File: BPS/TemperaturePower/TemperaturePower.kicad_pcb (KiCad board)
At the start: 2 copper layers, 35 x 44 mm, 7 parts, among them J1 Conn_02x10_Counter_Clockwise, J2 Conn_01x02, J3 Conn_02x10_Counter_Clockwise

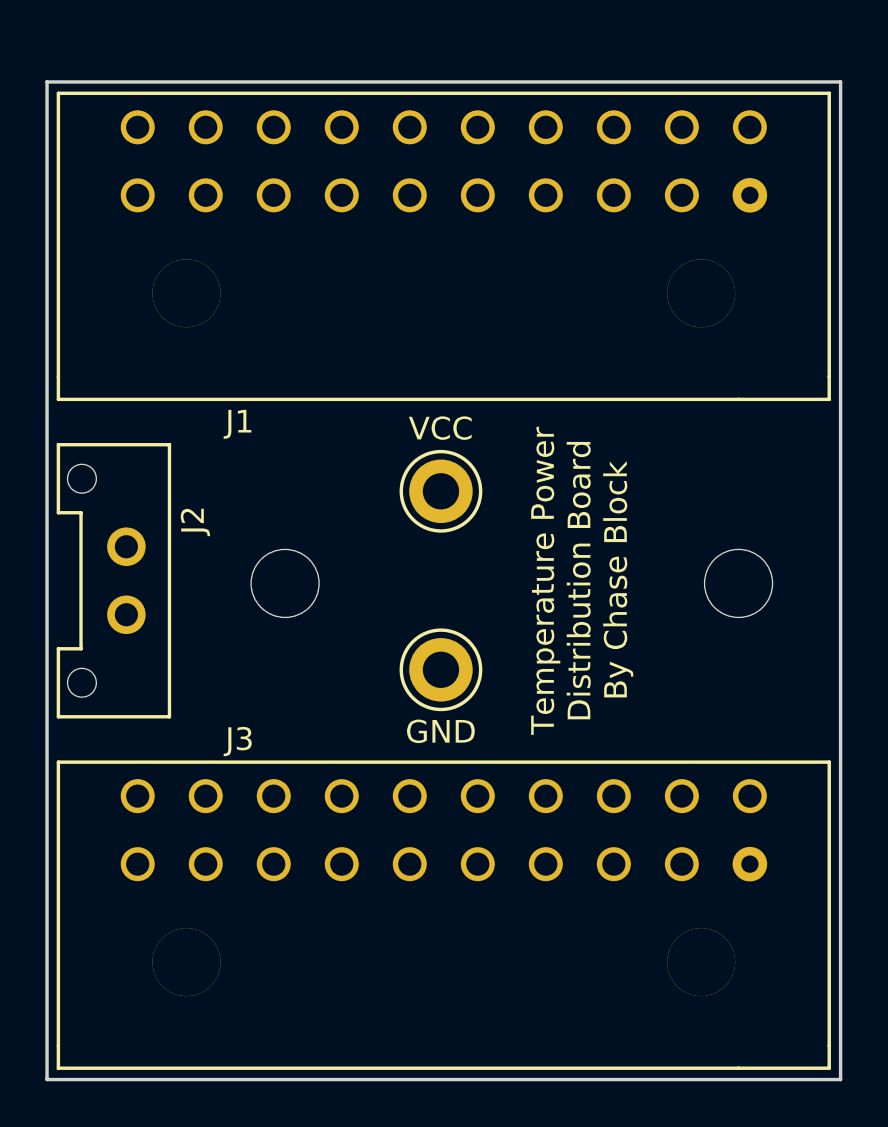
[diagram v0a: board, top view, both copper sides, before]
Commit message: Fix the backwardness to the Temperature power board
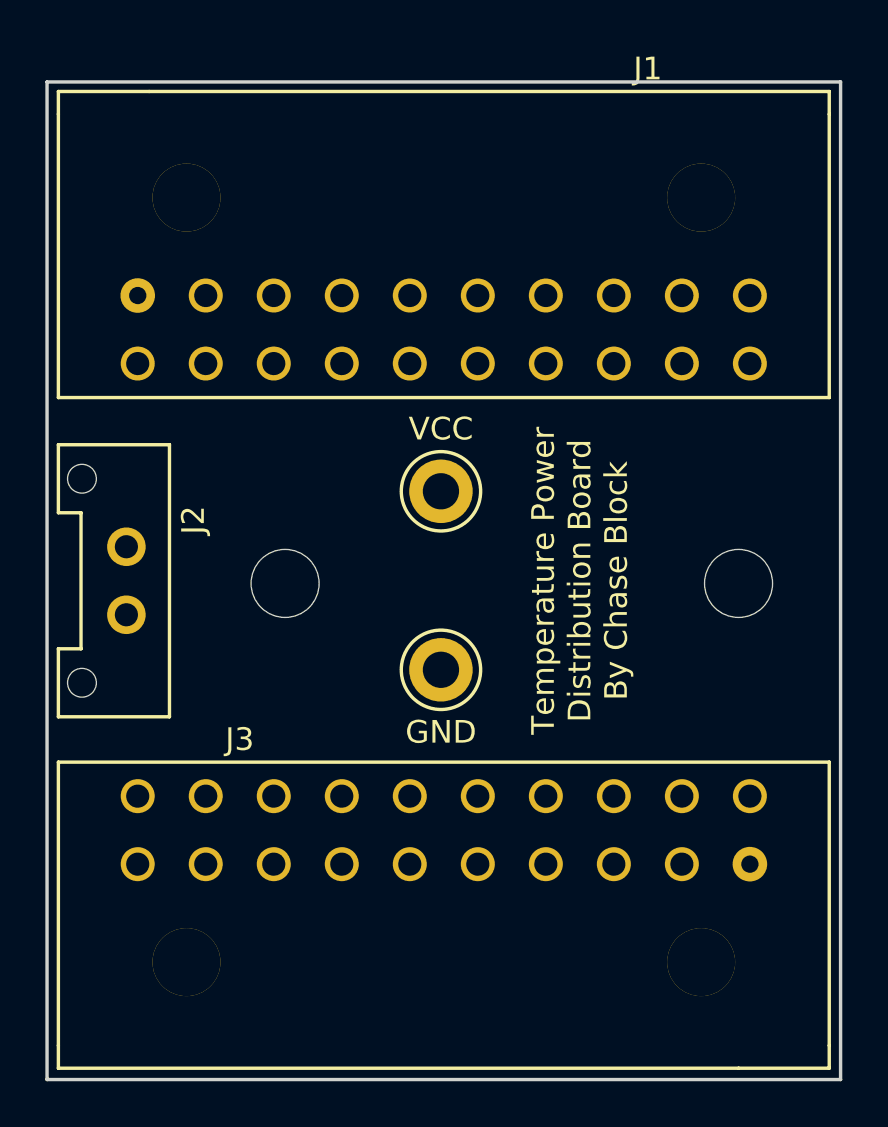
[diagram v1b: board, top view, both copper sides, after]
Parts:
- moved J1 7.42 mm to (135.0, 107.4), turned to 180 degrees
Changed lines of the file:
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@@
-(kicad_pcb (version 20171130) (host pcbnew "(5.1.4)-1")
+(kicad_pcb (version 20171130) (host pcbnew 5.1.4-e60b266~84~ubuntu19.04.1)
   (general
     (thickness 1.6)
@@
   )
   (module UTSVT_Connectors:Molex2x10_horizontal (layer F.Cu)
-    (at 135 100)
+    (at 135 107.42 180)
     (fp_text reference J1 (at -9 11.5) (layer F.SilkS)
       (effects (font (size 1 1) (thickness 0.15)))
@@
     (fp_line (start 13 10.5) (end -17 10.5) (layer F.SilkS) (width 0.15))
     (fp_line (start -17 10.5) (end -17 9.5) (layer F.SilkS) (width 0.15))
-    (pad 1 thru_hole circle (at 13.5 1.5) (size 1.524 1.524) (drill 0.762) (layers *.Cu *.Mask)
+    (pad 1 thru_hole circle (at 13.5 1.5 180) (size 1.524 1.524) (drill 0.762) (layers *.Cu *.Mask)
       (net 1 VCC))
-    (pad 2 thru_hole circle (at 10.5 1.5) (size 1.5 1.5) (drill 1.02) (layers *.Cu *.Mask)
+    (pad 2 thru_hole circle (at 10.5 1.5 180) (size 1.5 1.5) (drill 1.02) (layers *.Cu *.Mask)
       (net 1 VCC))
-    (pad 3 thru_hole circle (at 7.5 1.5) (size 1.5 1.5) (drill 1.02) (layers *.Cu *.Mask)
+    (pad 3 thru_hole circle (at 7.5 1.5 180) (size 1.5 1.5) (drill 1.02) (layers *.Cu *.Mask)
       (net 1 VCC))
-    (pad 4 thru_hole circle (at 4.5 1.5) (size 1.5 1.5) (drill 1.02) (layers *.Cu *.Mask)
+    (pad 4 thru_hole circle (at 4.5 1.5 180) (size 1.5 1.5) (drill 1.02) (layers *.Cu *.Mask)
       (net 1 VCC))
-    (pad 5 thru_hole circle (at 1.5 1.5) (size 1.5 1.5) (drill 1.02) (layers *.Cu *.Mask)
+    (pad 5 thru_hole circle (at 1.5 1.5 180) (size 1.5 1.5) (drill 1.02) (layers *.Cu *.Mask)
       (net 1 VCC))
-    (pad 6 thru_hole circle (at -1.5 1.5) (size 1.5 1.5) (drill 1.02) (layers *.Cu *.Mask)
+    (pad 6 thru_hole circle (at -1.5 1.5 180) (size 1.5 1.5) (drill 1.02) (layers *.Cu *.Mask)
       (net 1 VCC))
-    (pad 7 thru_hole circle (at -4.5 1.5) (size 1.5 1.5) (drill 1.02) (layers *.Cu *.Mask)
+    (pad 7 thru_hole circle (at -4.5 1.5 180) (size 1.5 1.5) (drill 1.02) (layers *.Cu *.Mask)
       (net 1 VCC))
-    (pad 8 thru_hole circle (at -7.5 1.5) (size 1.5 1.5) (drill 1.02) (layers *.Cu *.Mask)
+    (pad 8 thru_hole circle (at -7.5 1.5 180) (size 1.5 1.5) (drill 1.02) (layers *.Cu *.Mask)
       (net 1 VCC))
-    (pad 9 thru_hole circle (at -10.5 1.5) (size 1.5 1.5) (drill 1.02) (layers *.Cu *.Mask)
+    (pad 9 thru_hole circle (at -10.5 1.5 180) (size 1.5 1.5) (drill 1.02) (layers *.Cu *.Mask)
       (net 1 VCC))
-    (pad 10 thru_hole circle (at -13.5 1.5) (size 1.5 1.5) (drill 1.02) (layers *.Cu *.Mask)
+    (pad 10 thru_hole circle (at -13.5 1.5 180) (size 1.5 1.5) (drill 1.02) (layers *.Cu *.Mask)
       (net 1 VCC))
-    (pad 11 thru_hole circle (at 13.5 -1.5) (size 1.5 1.5) (drill 1.02) (layers *.Cu *.Mask)
+    (pad 11 thru_hole circle (at 13.5 -1.5 180) (size 1.5 1.5) (drill 1.02) (layers *.Cu *.Mask)
       (net 1 VCC))
-    (pad 12 thru_hole circle (at 10.5 -1.5) (size 1.5 1.5) (drill 1.02) (layers *.Cu *.Mask)
+    (pad 12 thru_hole circle (at 10.5 -1.5 180) (size 1.5 1.5) (drill 1.02) (layers *.Cu *.Mask)
       (net 1 VCC))
-    (pad 13 thru_hole circle (at 7.5 -1.5) (size 1.5 1.5) (drill 1.02) (layers *.Cu *.Mask)
+    (pad 13 thru_hole circle (at 7.5 -1.5 180) (size 1.5 1.5) (drill 1.02) (layers *.Cu *.Mask)
       (net 1 VCC))
-    (pad 14 thru_hole circle (at 4.5 -1.5) (size 1.5 1.5) (drill 1.02) (layers *.Cu *.Mask)
+    (pad 14 thru_hole circle (at 4.5 -1.5 180) (size 1.5 1.5) (drill 1.02) (layers *.Cu *.Mask)
       (net 1 VCC))
-    (pad 15 thru_hole circle (at 1.5 -1.5) (size 1.5 1.5) (drill 1.02) (layers *.Cu *.Mask)
+    (pad 15 thru_hole circle (at 1.5 -1.5 180) (size 1.5 1.5) (drill 1.02) (layers *.Cu *.Mask)
       (net 1 VCC))
-    (pad 16 thru_hole circle (at -1.5 -1.5) (size 1.5 1.5) (drill 1.02) (layers *.Cu *.Mask)
+    (pad 16 thru_hole circle (at -1.5 -1.5 180) (size 1.5 1.5) (drill 1.02) (layers *.Cu *.Mask)
       (net 1 VCC))
-    (pad 17 thru_hole circle (at -4.5 -1.5) (size 1.5 1.5) (drill 1.02) (layers *.Cu *.Mask)
+    (pad 17 thru_hole circle (at -4.5 -1.5 180) (size 1.5 1.5) (drill 1.02) (layers *.Cu *.Mask)
       (net 1 VCC))
-    (pad 18 thru_hole circle (at -7.5 -1.5) (size 1.5 1.5) (drill 1.02) (layers *.Cu *.Mask)
+    (pad 18 thru_hole circle (at -7.5 -1.5 180) (size 1.5 1.5) (drill 1.02) (layers *.Cu *.Mask)
       (net 1 VCC))
-    (pad 19 thru_hole circle (at -10.5 -1.5) (size 1.5 1.5) (drill 1.02) (layers *.Cu *.Mask)
+    (pad 19 thru_hole circle (at -10.5 -1.5 180) (size 1.5 1.5) (drill 1.02) (layers *.Cu *.Mask)
       (net 1 VCC))
-    (pad 20 thru_hole circle (at -13.5 -1.5) (size 1.5 1.5) (drill 1.02) (layers *.Cu *.Mask)
+    (pad 20 thru_hole circle (at -13.5 -1.5 180) (size 1.5 1.5) (drill 1.02) (layers *.Cu *.Mask)
       (net 1 VCC))
-    (pad "" thru_hole circle (at 11.35 5.82) (size 3 3) (drill 3) (layers *.Cu *.Mask))
-    (pad "" thru_hole circle (at -11.35 5.82) (size 3 3) (drill 3) (layers *.Cu *.Mask))
+    (pad "" thru_hole circle (at 11.35 5.82 180) (size 3 3) (drill 3) (layers *.Cu *.Mask))
+    (pad "" thru_hole circle (at -11.35 5.82 180) (size 3 3) (drill 3) (layers *.Cu *.Mask))
   )
   (module UTSVT_Connectors:Molex_MicroFit3.0_1x2xP3.00mm_PolarizingPeg_Vertical (layer F.Cu)
